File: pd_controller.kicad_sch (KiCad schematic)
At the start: 29 parts, among them Q1 IRF9358TRPBF, Q2 BSL308PEH6327XTSA1, U2 CYPD3177-24LQXQT

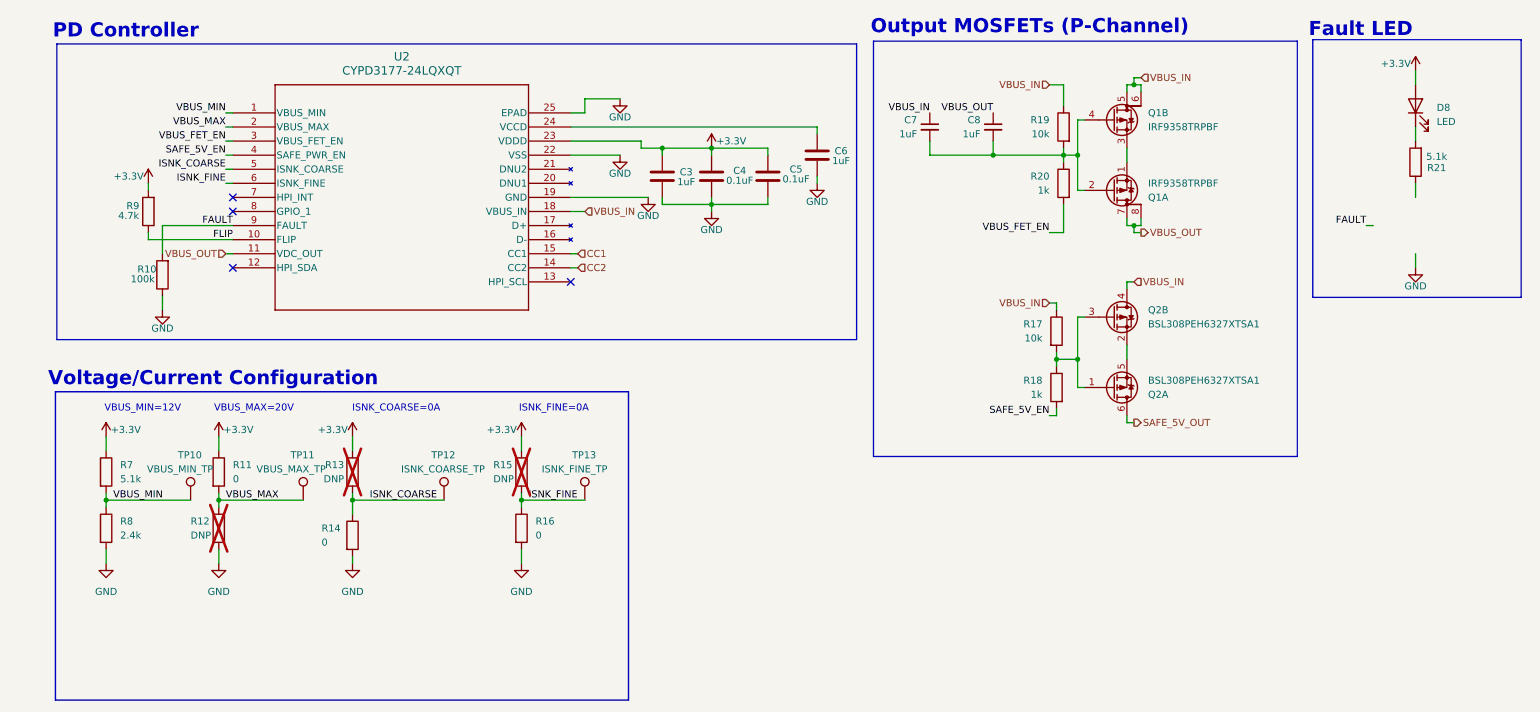
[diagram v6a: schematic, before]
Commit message: Addressed most of the review comments, fixed power protection, added bigger caps & better part selection on 12V and 5V out, changed 5V buck inductor, fixed power good & fault LEDs
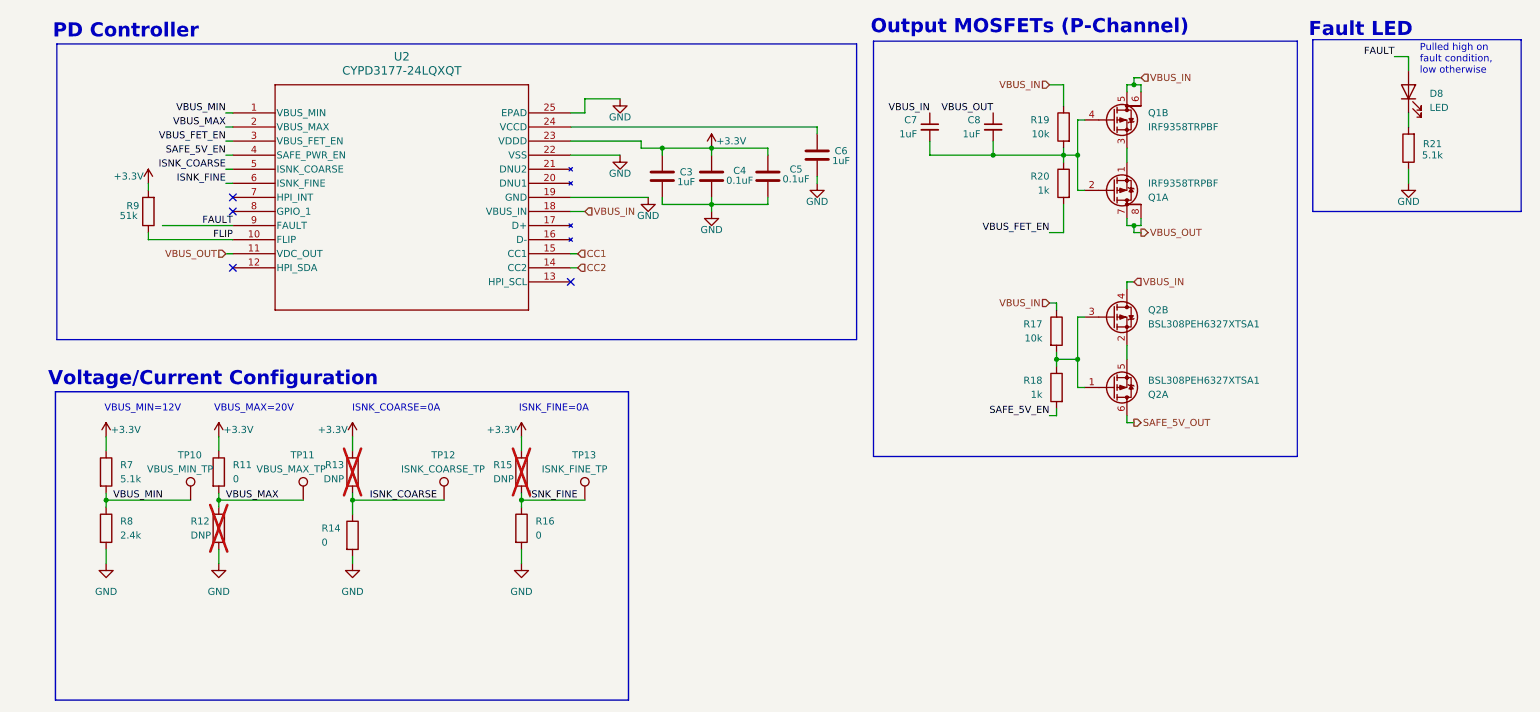
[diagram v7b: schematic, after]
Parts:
- removed R10: 100k, Resistor_SMD:R_0805_2012Metric, symbol Device:R
- R9: value 4.7k -> 51k; Mouser Part Number CRCW08054K70FKEAC -> CRCW080551K0FKEAC
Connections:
- net +3.3V: no longer D8.2 (A)
- net FAULT: now also D8.2 (A)
- net GND: now also R21.1
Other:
- note added: "Pulled high on fault condition, low otherwise"
- moved on the sheet: D8, R21

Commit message: Added ideal diode controller & mosfet for 12V buck power protection
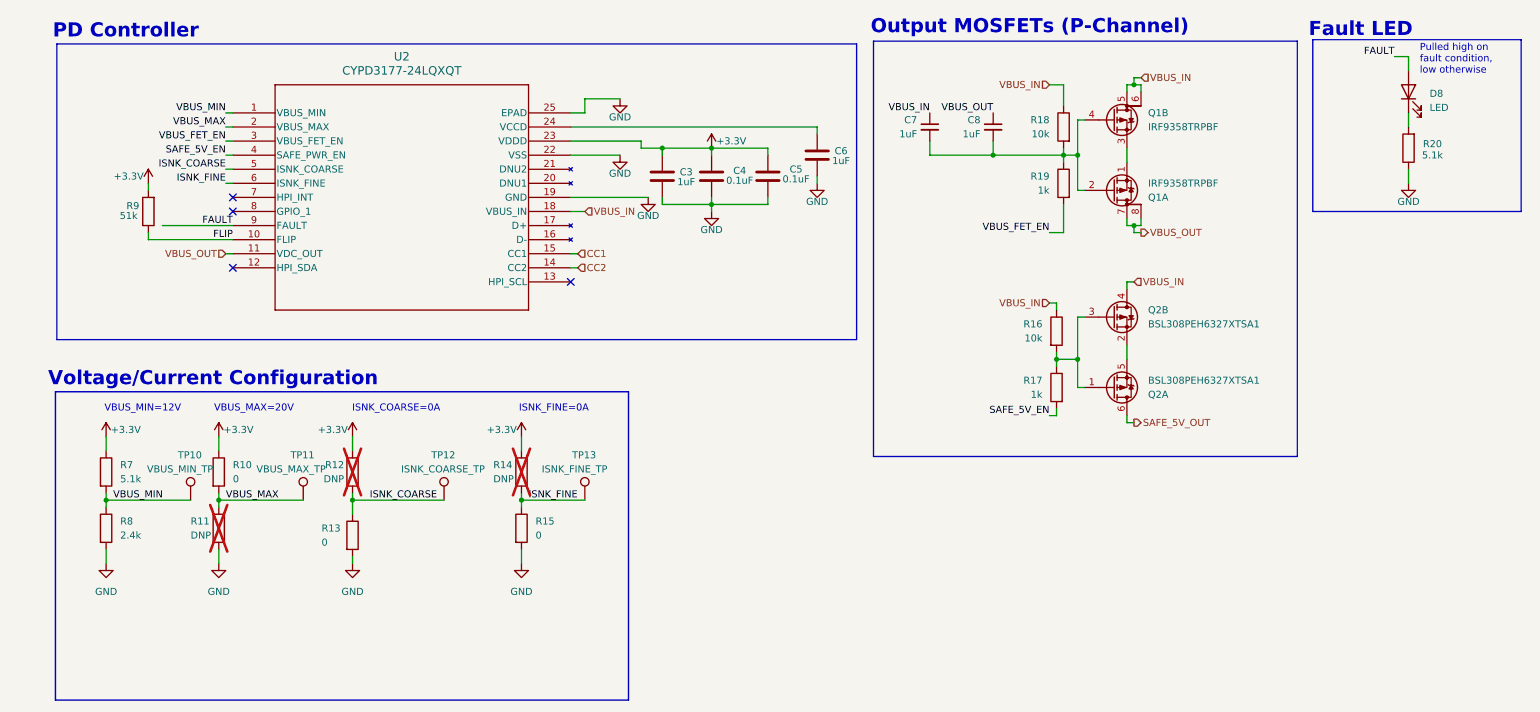
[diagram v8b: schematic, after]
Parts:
- Q1: Manufacturer_Name (none) -> Infineon; Mouser Part Number (none) -> IRF9358TRPBF
- Q2: Manufacturer_Name (none) -> Infineon; Mouser Part Number (none) -> BSL308PEH6327XTSA1
- renumbered R11 to R10, R12 to R11, R13 to R12, R14 to R13, R15 to R14, R16 to R15, R17 to R16, R18 to R17, R19 to R18, R20 to R19, R21 to R20
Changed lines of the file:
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@@
 		(on_board yes)
 		(dnp no)
-		(property "Reference" "#PWR043"
+		(property "Reference" "#PWR042"
 			(at 120.65 69.85 0)
 			(effects
@@
 			(project "USBCPowerPCB"
 				(path "/f58400c5-df4b-4929-8d2b-33c0fe23fcd9/4ed27f5f-caef-4817-8da2-6ac4f08dfb73"
-					(reference "#PWR043")
+					(reference "#PWR042")
 					(unit 1)
 				)
@@
 			)
 		)
+		(property "Manufacturer_Name" "Infineon"
+			(at 209.55 105.41 0)
+			(effects
+				(font
+					(size 1.27 1.27)
+				)
+				(hide yes)
+			)
+		)
+		(property "Mouser Part Number" "BSL308PEH6327XTSA1"
+			(at 209.55 105.41 0)
+			(effects
+				(font
+					(size 1.27 1.27)
+				)
+				(hide yes)
+			)
+		)
 		(pin "2"
 		)
@@
 		(dnp no)
 		(fields_autoplaced yes)
-		(property "Reference" "R19"
+		(property "Reference" "R18"
 			(at 198.12 57.1499 0)
 			(effects
@@
 			(project "USBCPowerPCB"
 				(path "/f58400c5-df4b-4929-8d2b-33c0fe23fcd9/4ed27f5f-caef-4817-8da2-6ac4f08dfb73"
-					(reference "R19")
+					(reference "R18")
 					(unit 1)
 				)
@@
 		(on_board yes)
 		(dnp no)
-		(property "Reference" "#PWR040"
+		(property "Reference" "#PWR039"
 			(at 102.87 118.11 0)
 			(effects
@@
 			(project "USBCPowerPCB"
 				(path "/f58400c5-df4b-4929-8d2b-33c0fe23fcd9/4ed27f5f-caef-4817-8da2-6ac4f08dfb73"
-					(reference "#PWR040")
+					(reference "#PWR039")
 					(unit 1)
 				)
@@
 		(dnp no)
 		(fields_autoplaced yes)
-		(property "Reference" "#PWR037"
+		(property "Reference" "#PWR036"
 			(at 48.26 143.51 0)
 			(effects
@@
 			(project "USBCPowerPCB"
 				(path "/f58400c5-df4b-4929-8d2b-33c0fe23fcd9/4ed27f5f-caef-4817-8da2-6ac4f08dfb73"
-					(reference "#PWR037")
+					(reference "#PWR036")
 					(unit 1)
 				)
@@
 		(on_board yes)
 		(dnp no)
-		(property "Reference" "#PWR046"
+		(property "Reference" "#PWR045"
 			(at 137.16 80.01 0)
 			(effects
@@
 			(project "USBCPowerPCB"
 				(path "/f58400c5-df4b-4929-8d2b-33c0fe23fcd9/4ed27f5f-caef-4817-8da2-6ac4f08dfb73"
-					(reference "#PWR046")
+					(reference "#PWR045")
 					(unit 1)
 				)
@@
 		(on_board yes)
 		(dnp no)
-		(property "Reference" "R14"
+		(property "Reference" "R13"
 			(at 66.802 130.81 0)
 			(effects
@@
 			(project "USBCPowerPCB"
 				(path "/f58400c5-df4b-4929-8d2b-33c0fe23fcd9/4ed27f5f-caef-4817-8da2-6ac4f08dfb73"
-					(reference "R14")
+					(reference "R13")
 					(unit 1)
 				)
@@
 			)
 		)
+		(property "Manufacturer_Name" "Infineon"
+			(at 209.55 92.71 0)
+			(effects
+				(font
+					(size 1.27 1.27)
+				)
+				(hide yes)
+			)
+		)
+		(property "Mouser Part Number" "BSL308PEH6327XTSA1"
+			(at 209.55 92.71 0)
+			(effects
+				(font
+					(size 1.27 1.27)
+				)
+				(hide yes)
+			)
+		)
 		(pin "2"
 		)
@@
 		(on_board yes)
 		(dnp no)
-		(property "Reference" "#PWR044"
+		(property "Reference" "#PWR043"
 			(at 125.73 77.47 0)
 			(effects
@@
 			(project "USBCPowerPCB"
 				(path "/f58400c5-df4b-4929-8d2b-33c0fe23fcd9/4ed27f5f-caef-4817-8da2-6ac4f08dfb73"
-					(reference "#PWR044")
+					(reference "#PWR043")
 					(unit 1)
 				)
@@
 		(on_board yes)
 		(dnp yes)
-		(property "Reference" "R13"
+		(property "Reference" "R12"
 			(at 70.866 119.38 0)
 			(effects
@@
 			(project "USBCPowerPCB"
 				(path "/f58400c5-df4b-4929-8d2b-33c0fe23fcd9/4ed27f5f-caef-4817-8da2-6ac4f08dfb73"
-					(reference "R13")
+					(reference "R12")
 					(unit 1)
 				)
@@
 		(on_board yes)
 		(dnp yes)
-		(property "Reference" "R15"
+		(property "Reference" "R14"
 			(at 97.79 119.38 0)
 			(effects
@@
 			(project "USBCPowerPCB"
 				(path "/f58400c5-df4b-4929-8d2b-33c0fe23fcd9/4ed27f5f-caef-4817-8da2-6ac4f08dfb73"
-					(reference "R15")
+					(reference "R14")
 					(unit 1)
 				)
@@
 		(dnp no)
 		(fields_autoplaced yes)
-		(property "Reference" "#PWR039"
+		(property "Reference" "#PWR038"
 			(at 72.39 143.51 0)
 			(effects
@@
 			(project "USBCPowerPCB"
 				(path "/f58400c5-df4b-4929-8d2b-33c0fe23fcd9/4ed27f5f-caef-4817-8da2-6ac4f08dfb73"
-					(reference "#PWR039")
+					(reference "#PWR038")
 					(unit 1)
 				)
@@
 		(on_board yes)
 		(dnp no)
-		(property "Reference" "#PWR042"
+		(property "Reference" "#PWR041"
 			(at 120.65 59.69 0)
 			(effects
@@
 			(project "USBCPowerPCB"
 				(path "/f58400c5-df4b-4929-8d2b-33c0fe23fcd9/4ed27f5f-caef-4817-8da2-6ac4f08dfb73"
-					(reference "#PWR042")
+					(reference "#PWR041")
 					(unit 1)
 				)
@@
 		(on_board yes)
 		(dnp yes)
-		(property "Reference" "R12"
+		(property "Reference" "R11"
 			(at 43.18 129.54 0)
 			(effects
@@
 			(project "USBCPowerPCB"
 				(path "/f58400c5-df4b-4929-8d2b-33c0fe23fcd9/4ed27f5f-caef-4817-8da2-6ac4f08dfb73"
-					(reference "R12")
+					(reference "R11")
 					(unit 1)
 				)
@@
 		(on_board yes)
 		(dnp no)
-		(property "Reference" "R17"
+		(property "Reference" "R16"
 			(at 196.85 93.9799 0)
 			(effects
@@
 			(project "USBCPowerPCB"
 				(path "/f58400c5-df4b-4929-8d2b-33c0fe23fcd9/4ed27f5f-caef-4817-8da2-6ac4f08dfb73"
-					(reference "R17")
+					(reference "R16")
 					(unit 1)
 				)
@@
 			)
 		)
+		(property "Manufacturer_Name" "Infineon"
+			(at 209.55 57.15 0)
+			(effects
+				(font
+					(size 1.27 1.27)
+				)
+				(hide yes)
+			)
+		)
+		(property "Mouser Part Number" "IRF9358TRPBF"
+			(at 209.55 57.15 0)
+			(effects
+				(font
+					(size 1.27 1.27)
+				)
+				(hide yes)
+			)
+		)
 		(pin "7"
 		)
@@
 		(on_board yes)
 		(dnp no)
-		(property "Reference" "#PWR047"
+		(property "Reference" "#PWR046"
 			(at 156.21 74.93 0)
 			(effects
@@
 			(project "USBCPowerPCB"
 				(path "/f58400c5-df4b-4929-8d2b-33c0fe23fcd9/4ed27f5f-caef-4817-8da2-6ac4f08dfb73"
-					(reference "#PWR047")
+					(reference "#PWR046")
 					(unit 1)
 				)
@@
 		(on_board yes)
 		(dnp no)
-		(property "Reference" "#PWR036"
+		(property "Reference" "#PWR035"
 			(at 48.26 118.11 0)
 			(effects
@@
 			(project "USBCPowerPCB"
 				(path "/f58400c5-df4b-4929-8d2b-33c0fe23fcd9/4ed27f5f-caef-4817-8da2-6ac4f08dfb73"
-					(reference "#PWR036")
+					(reference "#PWR035")
 					(unit 1)
 				)
@@
 		(on_board yes)
 		(dnp no)
-		(property "Reference" "#PWR045"
+		(property "Reference" "#PWR044"
 			(at 137.16 66.04 0)
 			(effects
@@
 			(project "USBCPowerPCB"
 				(path "/f58400c5-df4b-4929-8d2b-33c0fe23fcd9/4ed27f5f-caef-4817-8da2-6ac4f08dfb73"
-					(reference "#PWR045")
+					(reference "#PWR044")
 					(unit 1)
 				)
@@
 		(dnp no)
 		(fields_autoplaced yes)
-		(property "Reference" "R20"
+		(property "Reference" "R19"
 			(at 198.12 67.3099 0)
 			(effects
@@
 			(project "USBCPowerPCB"
 				(path "/f58400c5-df4b-4929-8d2b-33c0fe23fcd9/4ed27f5f-caef-4817-8da2-6ac4f08dfb73"
-					(reference "R20")
+					(reference "R19")
 					(unit 1)
 				)
@@
 		(dnp no)
 		(fields_autoplaced yes)
-		(property "Reference" "R18"
+		(property "Reference" "R17"
 			(at 196.85 104.1399 0)
 			(effects
@@
 			(project "USBCPowerPCB"
 				(path "/f58400c5-df4b-4929-8d2b-33c0fe23fcd9/4ed27f5f-caef-4817-8da2-6ac4f08dfb73"
-					(reference "R18")
+					(reference "R17")
 					(unit 1)
 				)
@@
 		(dnp no)
 		(fields_autoplaced yes)
-		(property "Reference" "R11"
+		(property "Reference" "R10"
 			(at 50.8 119.3799 0)
 			(effects
@@
 			(project "USBCPowerPCB"
 				(path "/f58400c5-df4b-4929-8d2b-33c0fe23fcd9/4ed27f5f-caef-4817-8da2-6ac4f08dfb73"
-					(reference "R11")
+					(reference "R10")
 					(unit 1)
 				)
@@
 		(dnp no)
 		(fields_autoplaced yes)
-		(property "Reference" "#PWR041"
+		(property "Reference" "#PWR040"
 			(at 102.87 143.51 0)
 			(effects
@@
 			(project "USBCPowerPCB"
 				(path "/f58400c5-df4b-4929-8d2b-33c0fe23fcd9/4ed27f5f-caef-4817-8da2-6ac4f08dfb73"
-					(reference "#PWR041")
+					(reference "#PWR040")
 					(unit 1)
 				)
@@
 		(dnp no)
 		(fields_autoplaced yes)
-		(property "Reference" "R16"
+		(property "Reference" "R15"
 			(at 105.41 129.5399 0)
 			(effects
@@
 			(project "USBCPowerPCB"
 				(path "/f58400c5-df4b-4929-8d2b-33c0fe23fcd9/4ed27f5f-caef-4817-8da2-6ac4f08dfb73"
-					(reference "R16")
+					(reference "R15")
 					(unit 1)
 				)
@@
 		(on_board yes)
 		(dnp no)
-		(property "Reference" "R21"
+		(property "Reference" "R20"
 			(at 267.208 61.468 0)
 			(effects
@@
 			(project "USBCPowerPCB"
 				(path "/f58400c5-df4b-4929-8d2b-33c0fe23fcd9/4ed27f5f-caef-4817-8da2-6ac4f08dfb73"
-					(reference "R21")
+					(reference "R20")
 					(unit 1)
 				)
@@
 			)
 		)
+		(property "Manufacturer_Name" "Infineon"
+			(at 209.55 69.85 0)
+			(effects
+				(font
+					(size 1.27 1.27)
+				)
+				(hide yes)
+			)
+		)
+		(property "Mouser Part Number" "IRF9358TRPBF"
+			(at 209.55 69.85 0)
+			(effects
+				(font
+					(size 1.27 1.27)
+				)
+				(hide yes)
+			)
+		)
 		(pin "7"
 		)
@@
 		(on_board yes)
 		(dnp no)
-		(property "Reference" "#PWR038"
+		(property "Reference" "#PWR037"
 			(at 72.39 118.11 0)
 			(effects
@@
 			(project "USBCPowerPCB"
 				(path "/f58400c5-df4b-4929-8d2b-33c0fe23fcd9/4ed27f5f-caef-4817-8da2-6ac4f08dfb73"
-					(reference "#PWR038")
+					(reference "#PWR037")
 					(unit 1)
 				)
@@
 		(on_board yes)
 		(dnp no)
-		(property "Reference" "#PWR049"
+		(property "Reference" "#PWR047"
 			(at 262.89 74.93 0)
 			(effects
@@
 			(project "USBCPowerPCB"
 				(path "/f58400c5-df4b-4929-8d2b-33c0fe23fcd9/4ed27f5f-caef-4817-8da2-6ac4f08dfb73"
-					(reference "#PWR049")
+					(reference "#PWR047")
 					(unit 1)
 				)
